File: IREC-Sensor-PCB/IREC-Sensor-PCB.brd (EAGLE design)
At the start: 65 x 56.5 mm, 9 parts, among them J1 RASPBERRYPI-40-PIN-GPIO_PTH_N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, J2 BME280-I2C, J3 BME280-SPI, J4 MPU6050

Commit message: Updated Sensor PCB files
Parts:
- removed J7, J8: (no value), SparkFun-Connectors:SCREWTERMINAL-3.5MM-4
- added D1: 200mA/100V/1V, SparkFun-DiscreteSemi:DIODE-1N4148
- added K1: RELAY-SPDT-JQX-15F, SparkFun-Electromechanical:RELAY-T90
- J1: value RASPBERRYPI-40-PIN-GPIO_PTH_NO_SHROUD -> (none); device SparkFun-Connectors:2X20 -> SparkFun-Connectors:1X07
- J2: value BME280-I2C -> (none); device SparkFun-Connectors:1X04_NO_SILK -> SparkFun-Connectors:1X06
- J3: value BME280-SPI -> (none); device SparkFun-Connectors:1X06_NO_SILK -> SparkFun-Connectors:1X04
- J4: value MPU6050 -> (none); device SparkFun-Connectors:1X10_NO_SILK -> SparkFun-Connectors:SCREWTERMINAL-3.5MM-4
- J5, J6: device SparkFun-Connectors:SCREWTERMINAL-3.5MM-4 -> SparkFun-Connectors:SCREWTERMINAL-3.5MM-2
- moved J4 52.7 mm to (-8.89, -38.1), turned to 0 degrees
- moved J6 44.3 mm to (-8.89, -86.4)
- moved J3 41.9 mm to (-10.2, -33.0)
- moved J2 35.8 mm to (-10.2, -29.2)
- moved J5 29.7 mm to (-8.89, -78.7)
- moved J1 27.6 mm to (-10.2, -25.4)
- moved FRAME1 23.6 mm to (8.89, -21.6)
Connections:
- removed net VDD: J1.1, J2.2, J4.1
- new net AD_AGM: J3.4
- new net AD_HPT: J1.5
- new net CS_HPT: J1.7
- new net INT: J3.3
- new net N$1: D1.A, J5.2, K1.COIL2
- new net N$2: D1.C, J5.1, K1.COIL1
- new net N$3: J6.2, K1.NO
- new net N$4: J6.1, K1.MAIN
- new net PS0: J3.1
- new net PS1: J3.2
- new net RST: J2.6
- net 3.3V: now also J1.2, J2.2; no longer J1.17
- net 5V: now also J1.1, J2.1, J4.2; no longer J1.2, J1.4
- net GND: now also J1.3, J2.3, J4.1; no longer J1.14, J1.20, J1.25, J1.30, J1.34, J1.39, J1.6, J1.9, J2.1, J4.2
- net SCL: now also J1.4, J2.5, J4.4; no longer J1.5, J2.4, J4.5
- net SDA: now also J1.6, J2.4, J4.3; no longer J1.3, J2.3, J4.6
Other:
- board outline removed
- board text added: "None Of Your Business Consulting"
- board text removed: "BME 280"
- board text removed: "MPU 6050"
- board text removed: "None Of Your Business consulting"

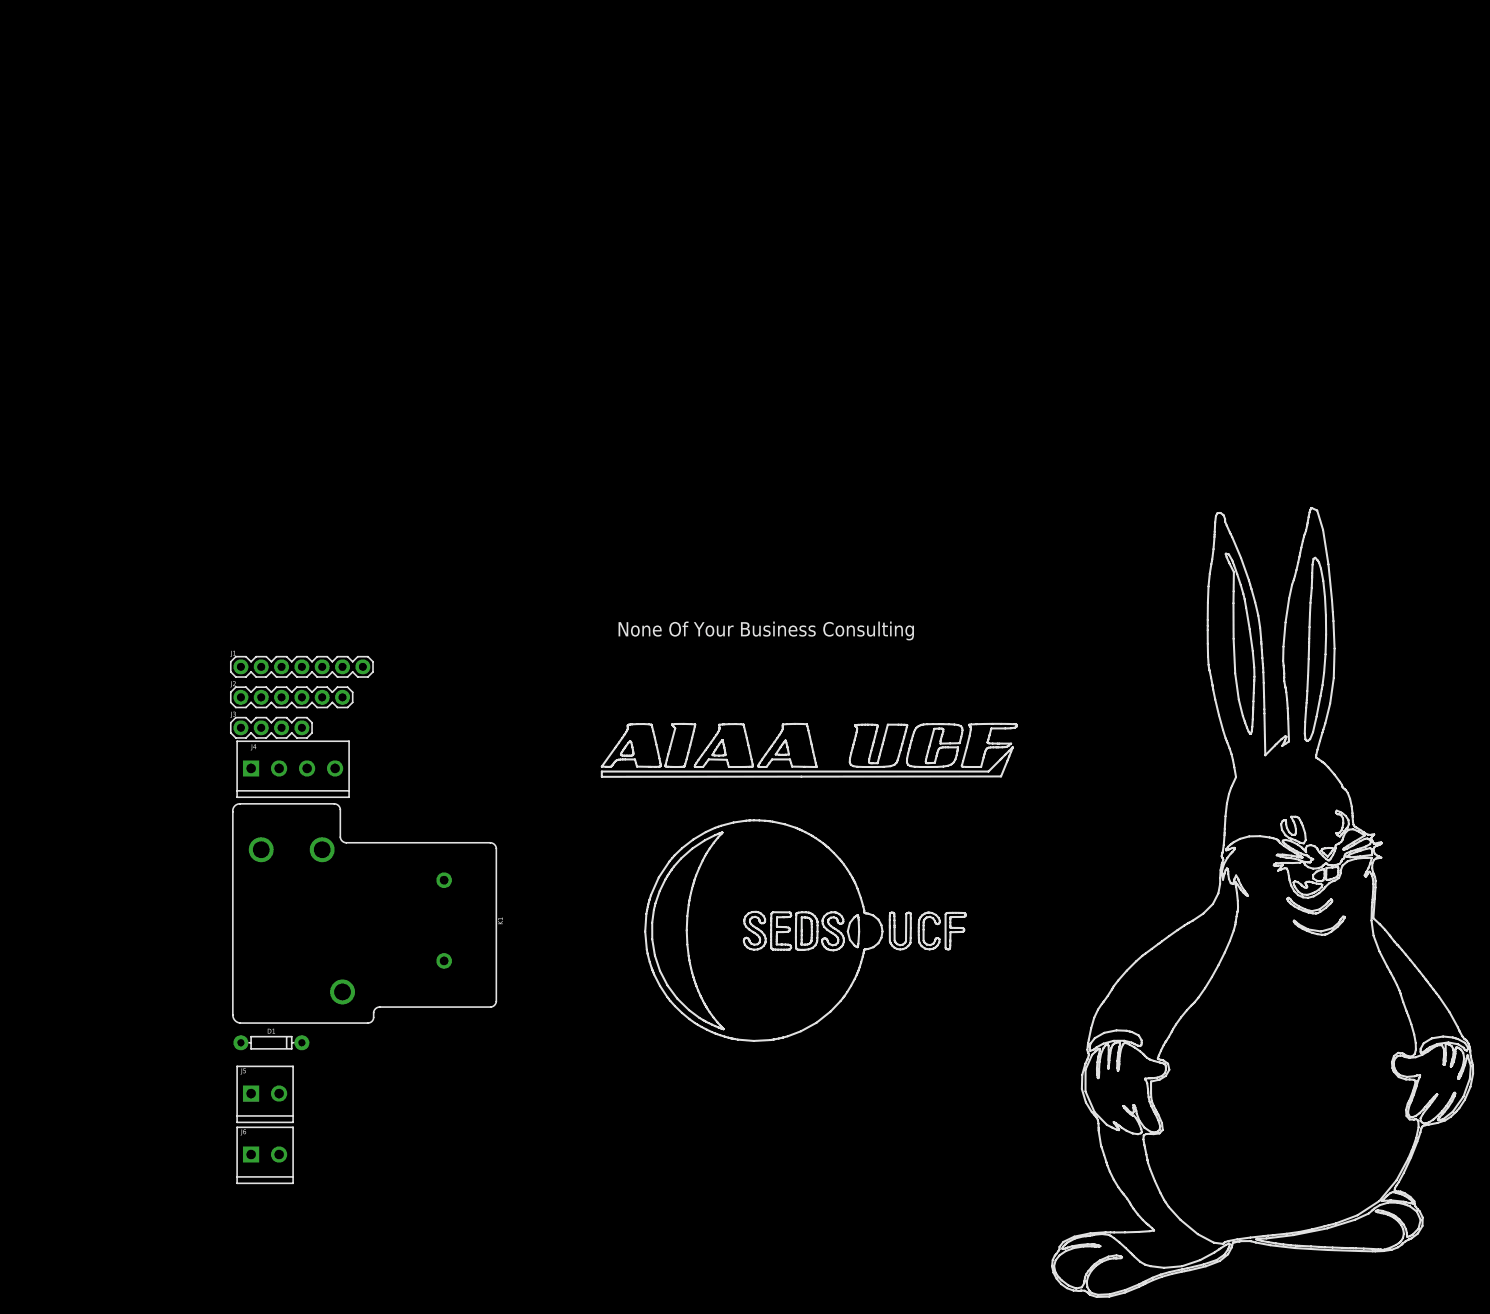
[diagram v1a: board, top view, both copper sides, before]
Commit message: Set up board dimensions
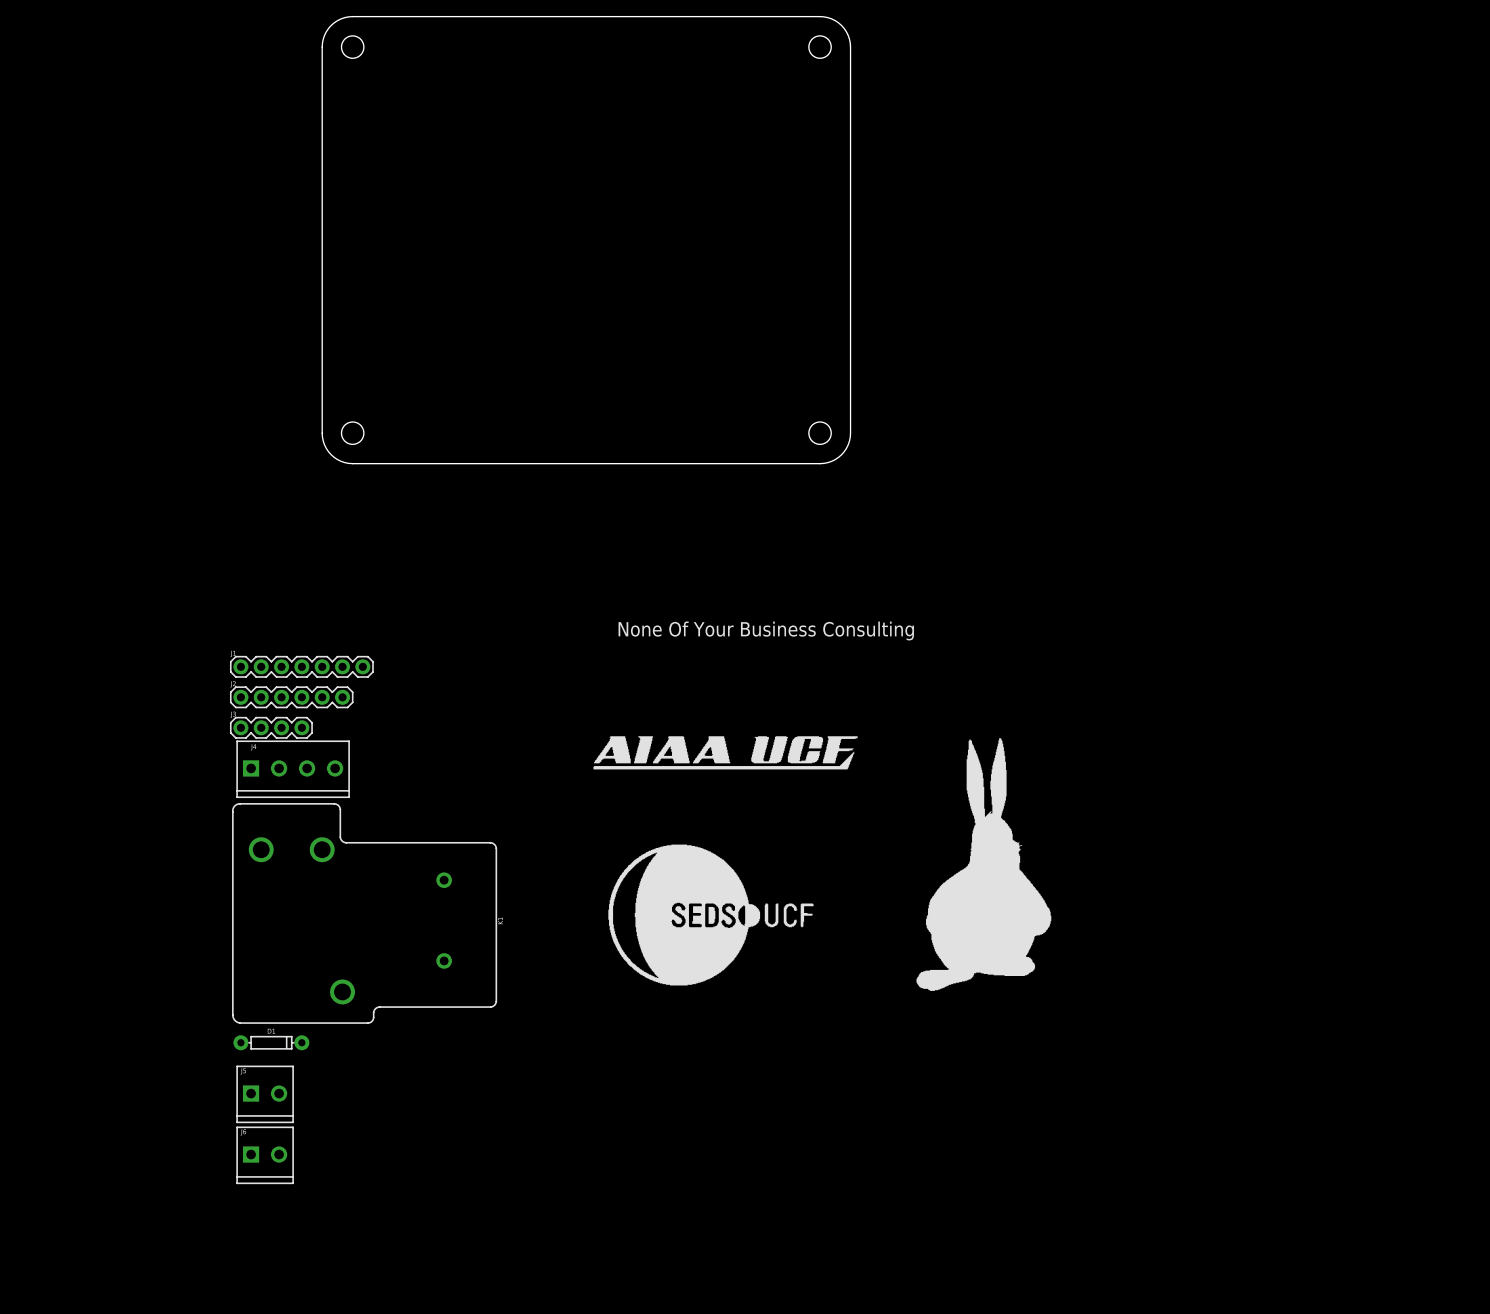
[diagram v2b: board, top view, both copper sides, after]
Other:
- board outline added: 66 x 55.9 mm

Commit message: Completed layout
Completed board layout
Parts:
- moved J6 96.1 mm to (-34.3, 6.35)
- moved D1 87.1 mm to (-17.8, 14.0), turned to 180 degrees
- moved J5 86.0 mm to (-21.6, 6.35)
- moved K1 80.2 mm to (-16.5, 25.4), turned to 270 degrees
- moved J3 80.2 mm to (29.2, 36.8)
- moved J1 75.0 mm to (48.3, 21.6)
- moved J2 60.7 mm to (26.7, 19.1)
- moved J4 55.8 mm to (27.9, 3.81)
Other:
- board text added: ""That'll hold them alright""
- board text added: "Big Chungus Sensor Board"
- board text added: "Version 1.0.0"

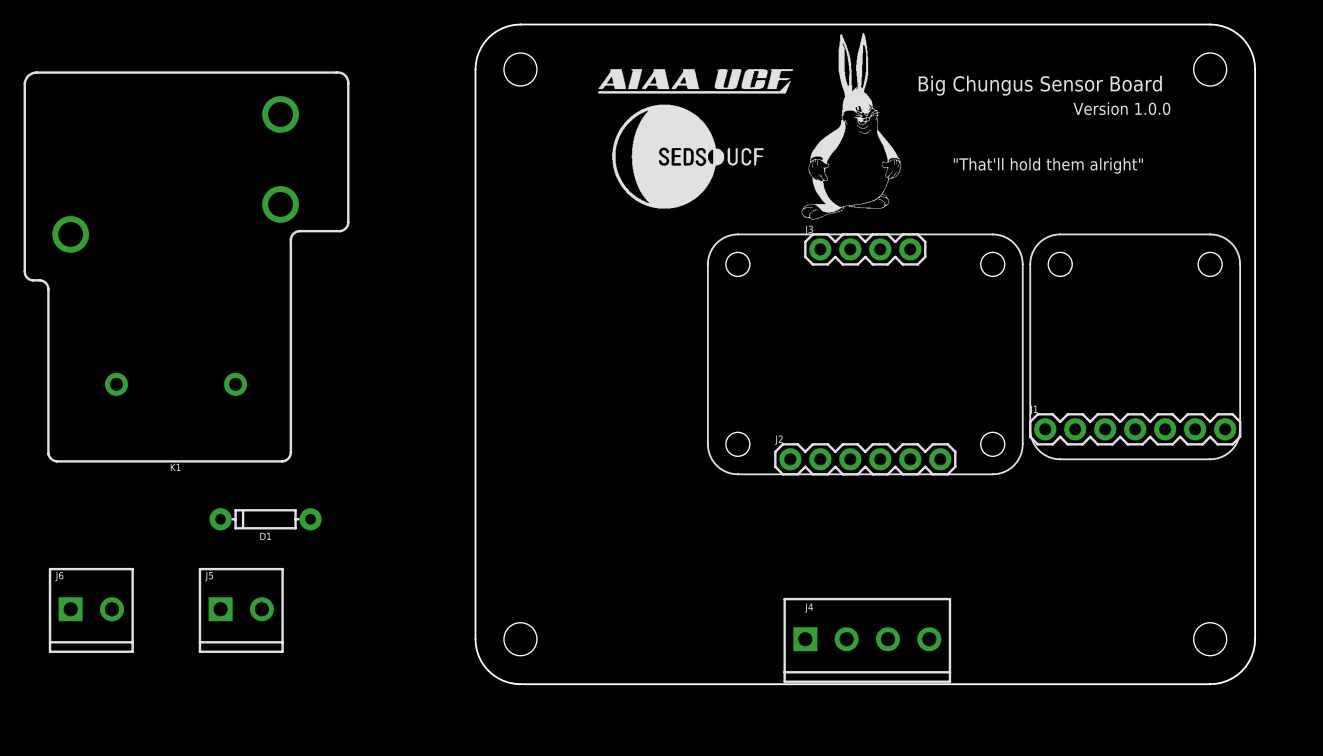
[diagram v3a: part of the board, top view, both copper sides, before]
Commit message: Final 1.0.0 Board!
Board is complete!
- Adjusted board dimensions
- Added relay
- Added I2C address switches
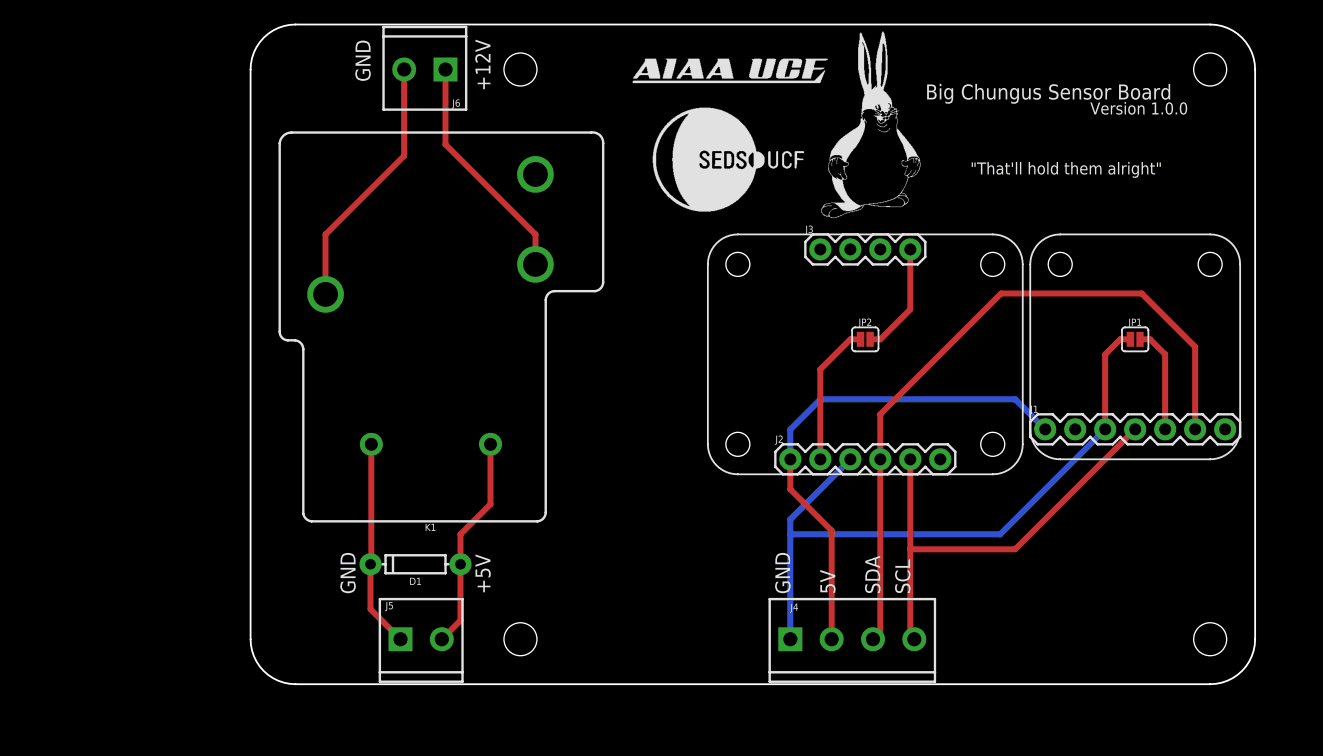
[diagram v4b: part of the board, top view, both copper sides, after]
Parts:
- added JP1: HPT_ADDR, SparkFun-Jumpers:SMT-JUMPER_2_NO_SILK
- added JP2: AGM_ADDR, SparkFun-Jumpers:SMT-JUMPER_2_NO_SILK
- moved J6 55.7 mm to (-2.54, 52.1), turned to 180 degrees
- moved K1 22.2 mm to (5.08, 20.3)
- moved J5 15.5 mm to (-6.35, 3.81)
- moved D1 13.3 mm to (-5.08, 10.2)
- moved J4 1.27 mm to (26.7, 3.81)
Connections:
- removed net 3.3V: J1.2, J2.2
- new net 3V_AGM: J2.2, JP2.1
- new net 3V_HPT: J1.2
- net AD_AGM: now also JP2.2
- net AD_HPT: now also JP1.2
- net GND: now also JP1.1
- net N$3: now also K1.MAIN; no longer K1.NO
- net N$4: now also K1.NO; no longer K1.MAIN
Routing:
- net SDA: track 0.00 -> 59.1 mm
- net GND: track 0.00 -> 56.7 mm
- net 5V: track 0.00 -> 42.9 mm
- net SCL: track 0.00 -> 38.6 mm
- net N$3: track 0.00 -> 21.8 mm
- net N$4: track 0.00 -> 19.7 mm
- net N$1: track 0.00 -> 18.2 mm
- net N$2: track 0.00 -> 17.6 mm
- net 3V_AGM: track 0.00 -> 12.1 mm
- net AD_AGM: track 0.00 -> 9.54 mm
- net AD_HPT: track 0.00 -> 9.01 mm
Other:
- board size 66 x 55.9 mm -> 85.1 x 55.9 mm
- board text added: "+12V"
- board text added: "+5V"
- board text added: "5V"
- board text added: "GND"
- board text added: "SCL"
- board text added: "SDA"
